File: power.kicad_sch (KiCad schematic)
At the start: 53 parts, among them J1 USB_C_Receptacle_USB2.0_16P, U1 TPS61088RHLT, U2 MCP73871, U3 AP2112K-3.3, U4 MAX17048G_T10, U5 USBLC6-2SC6

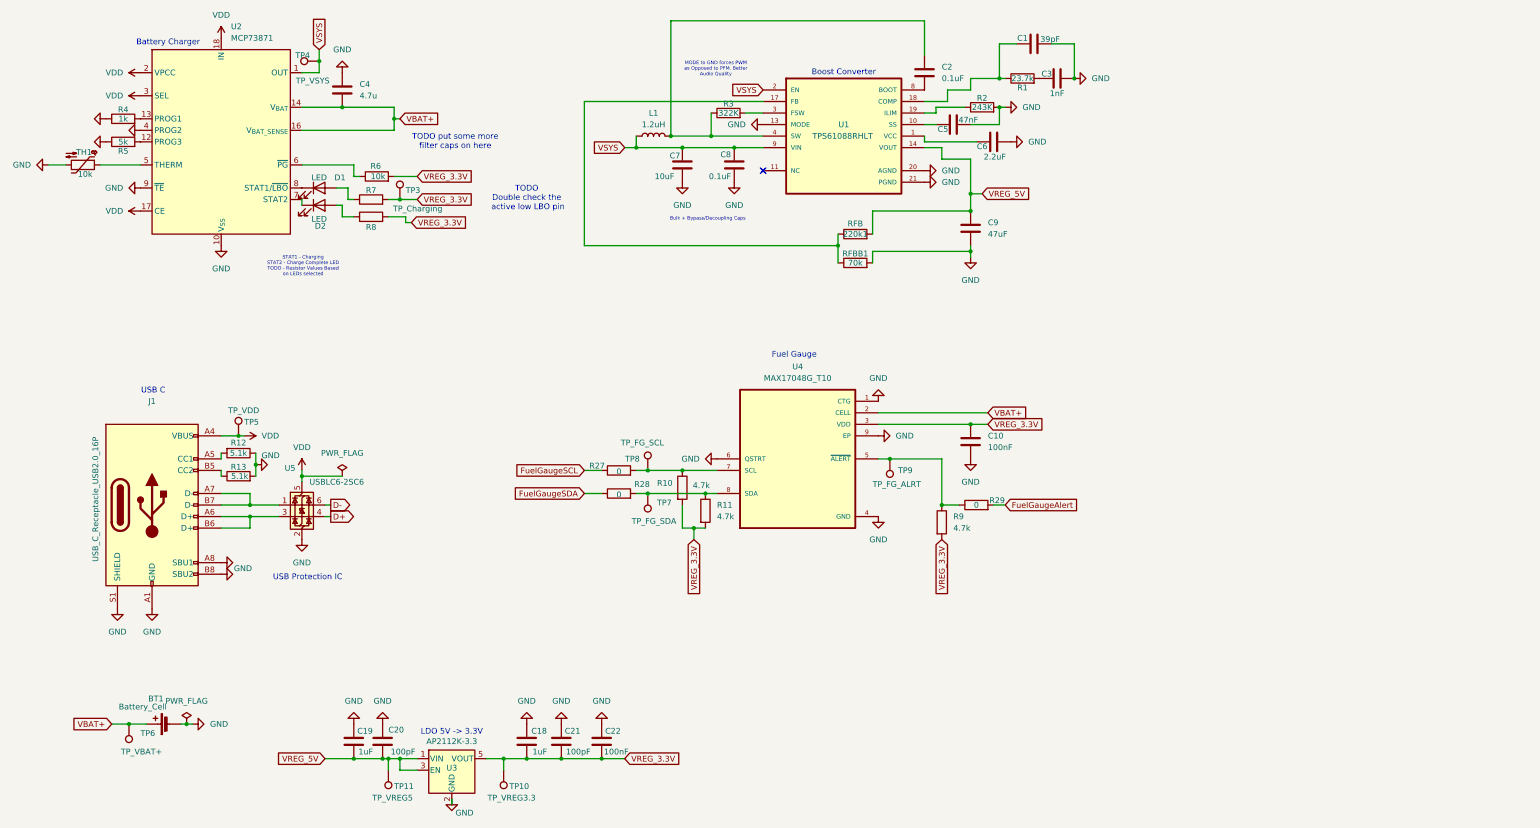
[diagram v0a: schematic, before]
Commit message: Remove Boost
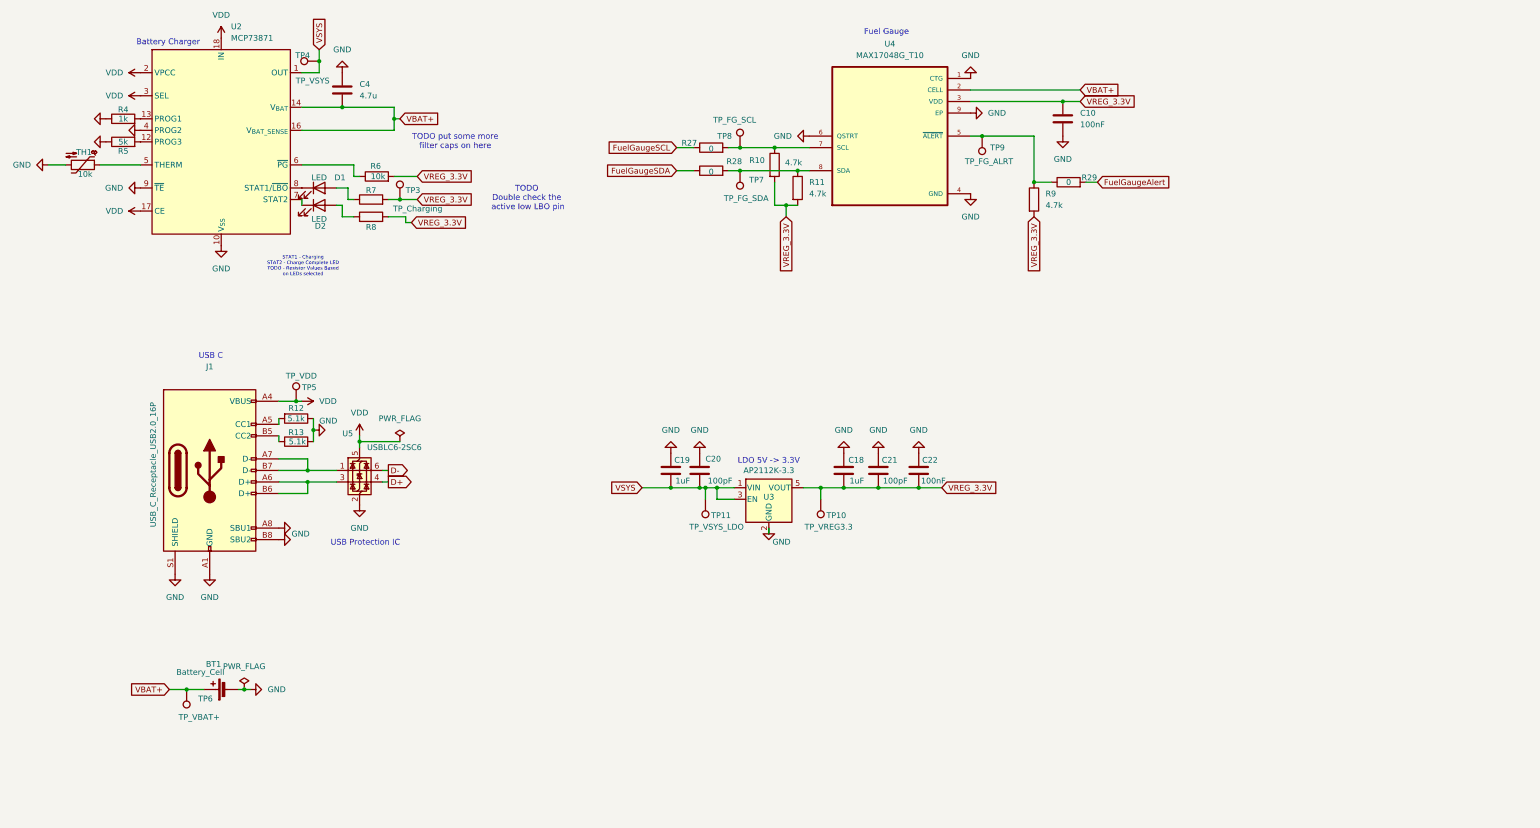
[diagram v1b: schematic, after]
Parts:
- removed 220k1: RFB, Resistor_SMD:R_0603_1608Metric_Pad0.98x0.95mm_HandSolder, symbol Device:R
- removed C1: 39pF, Capacitor_SMD:C_0603_1608Metric_Pad1.08x0.95mm_HandSolder, symbol Device:C
- removed C2, C8: 0.1uF, Capacitor_SMD:C_0603_1608Metric_Pad1.08x0.95mm_HandSolder, symbol Device:C
- removed C3: 1nF, Capacitor_SMD:C_0603_1608Metric_Pad1.08x0.95mm_HandSolder, symbol Device:C
- removed C5: 47nF, Capacitor_SMD:C_0603_1608Metric_Pad1.08x0.95mm_HandSolder, symbol Device:C
- removed C6: 2.2uF, Capacitor_SMD:C_0603_1608Metric_Pad1.08x0.95mm_HandSolder, symbol Device:C
- removed C7: 10uF, Capacitor_SMD:C_0603_1608Metric_Pad1.08x0.95mm_HandSolder, symbol Device:C
- removed C9: 47uF, Capacitor_SMD:C_0603_1608Metric_Pad1.08x0.95mm_HandSolder, symbol Device:C
- removed L1: 1.2uH, Inductor_SMD:L_0603_1608Metric_Pad1.05x0.95mm_HandSolder, symbol Device:L
- removed R1: 23.7k, Resistor_SMD:R_0603_1608Metric_Pad0.98x0.95mm_HandSolder, symbol Device:R
- removed R2: 243K, Resistor_SMD:R_0603_1608Metric_Pad0.98x0.95mm_HandSolder, symbol Device:R
- removed R3: 322K, Resistor_SMD:R_0603_1608Metric_Pad0.98x0.95mm_HandSolder, symbol Device:R
- removed RFBB1: 70k, Resistor_SMD:R_0603_1608Metric_Pad0.98x0.95mm_HandSolder, symbol Device:R
- removed U1: TPS61088RHLT, TPS61088RHLT:IC_MSP430FR2522IRHLR, symbol TPS61088:TPS61088RHLT
- TP11: value TP_VREG5 -> TP_VSYS_LDO
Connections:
- net VREG_5V is gone; now on net VSYS: C19.2, C20.2, TP11.1, U3.1 (VIN), U3.3 (EN)
- no-connect marks 1 -> 0
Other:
- note removed: "Boost Converter"
- note removed: "Bulk + Bypass/Decoupling Caps"
- note removed: "MODE to GND forces PWM as Opposed to PFM. Better Audio Quality"
- moved on the sheet: BT1, C10, C18, C19, C20, C21, C22, J1, R10, R11, R12, R13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

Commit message: Update USB C port and Charger to match App notes
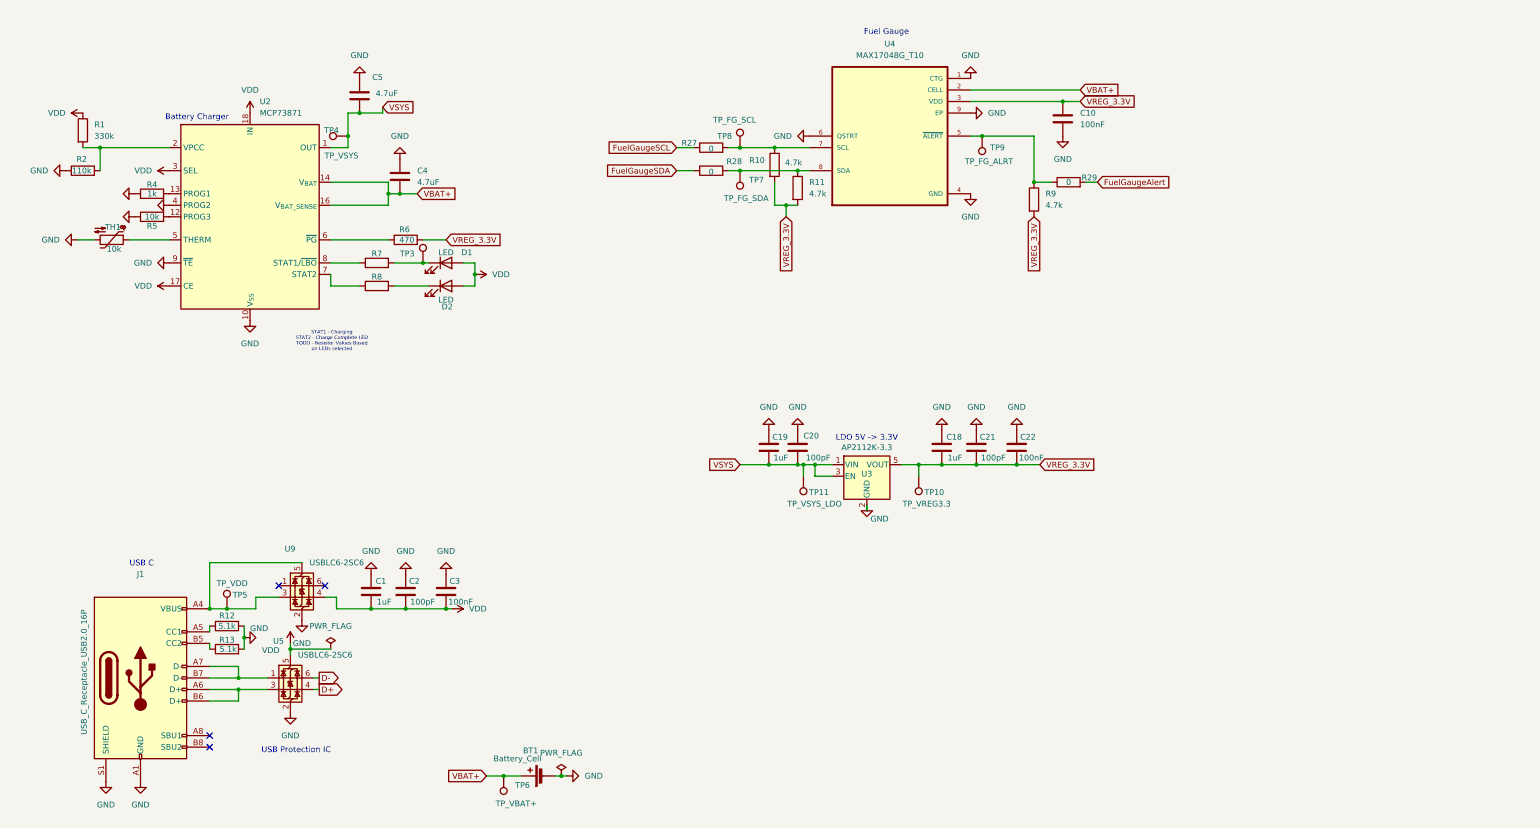
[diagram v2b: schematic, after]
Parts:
- added C1: 1uF, symbol Device:C
- added C2: 100pF, symbol Device:C
- added C3: 100nF, symbol Device:C
- added C5: 4.7uF, Capacitor_SMD:C_0603_1608Metric_Pad1.08x0.95mm_HandSolder, symbol Device:C
- added R1: 330k, symbol Device:R
- added R2: 110k, symbol Device:R
- added U9: USBLC6-2SC6, Package_TO_SOT_SMD:SOT-23-6, symbol Power_Protection:USBLC6-2SC6
- C4: value 4.7u -> 4.7uF
- R5: value 5k -> 10k
- R6: value 10k -> 470
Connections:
- net GND: now also C1.1, C2.1, C3.1, C5.2, R2.1, U9.2 (GND); no longer J1.A8 (SBU1), J1.B8 (SBU2)
- net VDD: now also D1.2 (A), D2.2 (A), C1.2, C2.2, C3.2, R1.1, U9.4 (I/O2); no longer J1.A4 (VBUS), J1.A9 (VBUS), J1.B4 (VBUS), J1.B9 (VBUS), TP5.1, U2.2 (VPCC)
- net VREG_3.3V: no longer R7.2, R8.2, TP3.1
- net VSYS: now also C5.1
- net at D1.1 (K): now also R7.2, TP3.1; no longer U2.8 (STAT1/~{LBO})
- net at R7.1: now also U2.8 (STAT1/~{LBO}); no longer D1.2 (A)
- net at D2.1 (K): now also R8.2; no longer U2.7 (STAT2)
- net at R8.1: now also U2.7 (STAT2); no longer D2.2 (A)
- new net: J1.A4 (VBUS), J1.A9 (VBUS), J1.B4 (VBUS), J1.B9 (VBUS), TP5.1, U9.3 (I/O2), U9.5 (VBUS)
- new net: R1.2, R2.2, U2.2 (VPCC)
- no-connect marks 0 -> 4
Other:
- note removed: "TODO Double check the active low LBO pin"
- note removed: "TODO put some more filter caps on here"
- moved on the sheet: BT1, C18, C19, C20, C21, C22, C4, D1, D2, J1, R12, R13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

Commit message: Finish power sheet
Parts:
- removed C10: 100nF, Capacitor_SMD:C_0603_1608Metric_Pad1.08x0.95mm_HandSolder, symbol Device:C
- removed C20: 100pF, symbol Device:C
- added C6: 0.1uF, Capacitor_SMD:C_0603_1608Metric_Pad1.08x0.95mm_HandSolder, symbol Device:C
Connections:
- net GND: now also C6.2
- net VBAT+: now also U4.3 (VDD), C6.1
- net VREG_3.3V: no longer U4.3 (VDD)

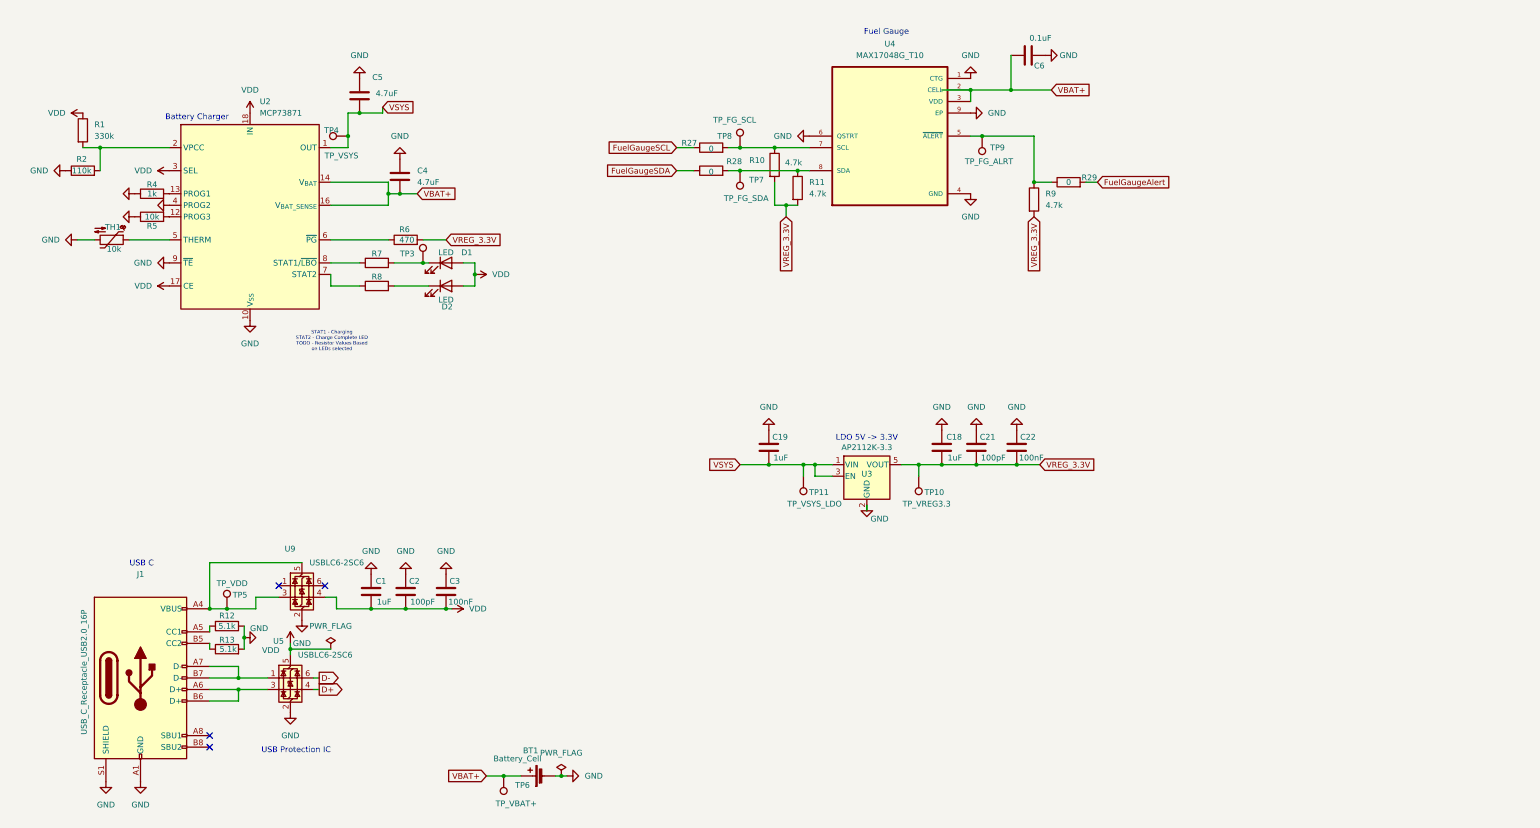
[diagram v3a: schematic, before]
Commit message: Update the USB-C symbol to match the actual part
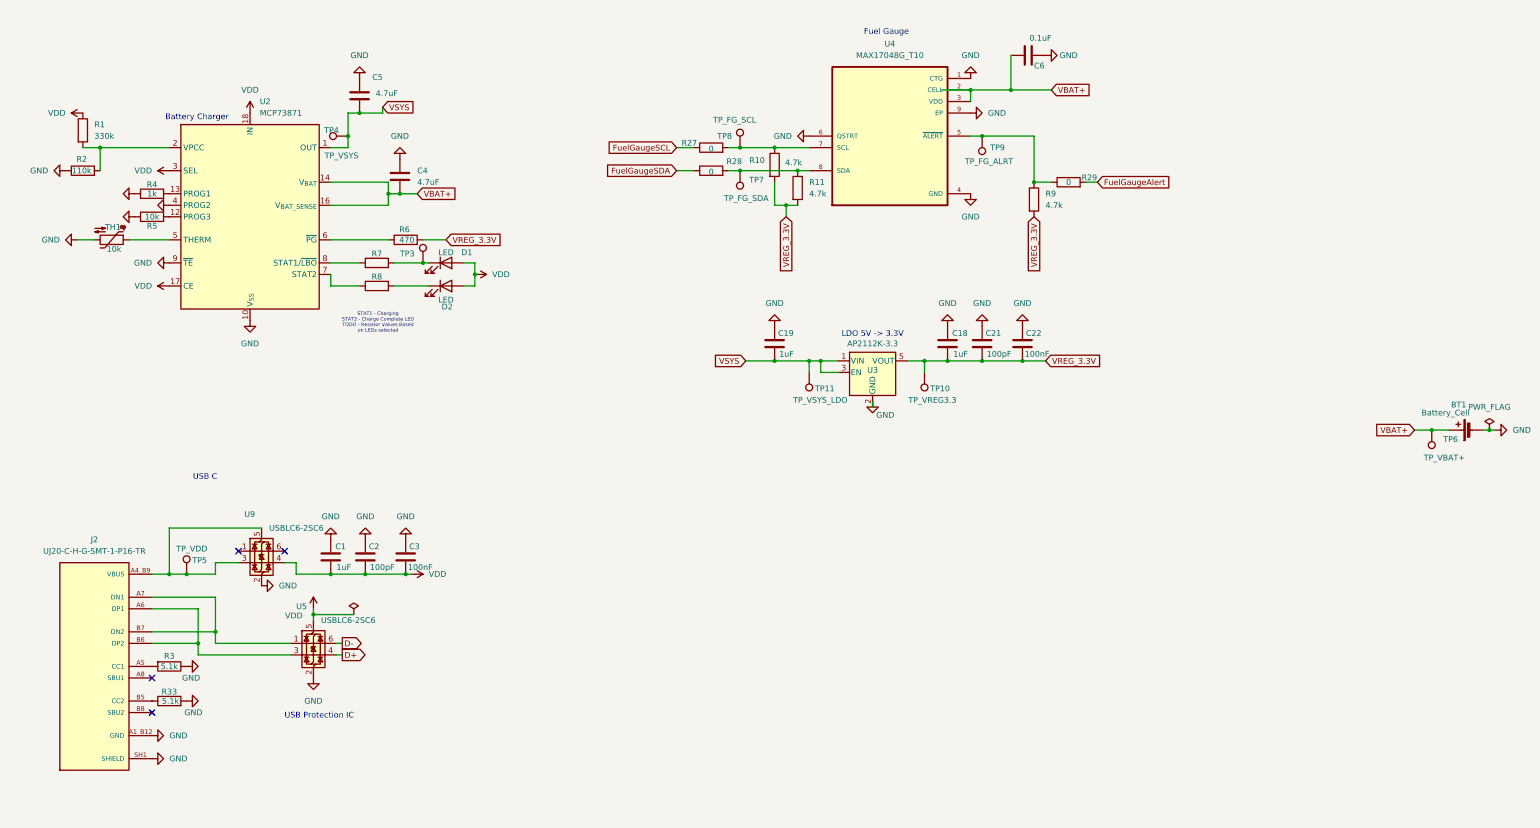
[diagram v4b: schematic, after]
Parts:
- removed J1: USB_C_Receptacle_USB2.0_16P, UJ20-C-H-G-SMT-1-P16-TR:SAMESKY_UJ20-C-H-G-SMT-1-P16-TR, symbol Connector:USB_C_Receptacle_USB2.0_16P
- removed R12, R13: 5.1k, Resistor_SMD:R_0603_1608Metric_Pad0.98x0.95mm_HandSolder, symbol Device:R
- added J2: UJ20-C-H-G-SMT-1-P16-TR, UJ20-C-H-G-SMT-1-P16-TR:SAMESKY_UJ20-C-H-G-SMT-1-P16-TR, symbol UJ20-C-H-G-SMT-1-P16-TR:UJ20-C-H-G-SMT-1-P16-TR
- added R3, R33: 5.1k, Resistor_SMD:R_0603_1608Metric_Pad0.98x0.95mm_HandSolder, symbol Device:R
- C1, C18, C19, C2, C21, C22, C3: footprint (none) -> Capacitor_SMD:C_0603_1608Metric_Pad1.08x0.95mm_HandSolder
- R1, R2, R27, R28, R29: footprint (none) -> Resistor_SMD:R_0603_1608Metric_Pad0.98x0.95mm_HandSolder
- TP10, TP11, TP3, TP4, TP5, TP6, TP7, TP8, TP9: footprint (none) -> TestPoint:TestPoint_Pad_D2.5mm
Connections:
- net GND: now also J2.A1_B12 (GND), J2.B1_A12 (GND), J2.SH1 (SHIELD), J2.SH2 (SHIELD), J2.SH3 (SHIELD), J2.SH4 (SHIELD), R3.1, R33.2
- net at TP5.1, U9.3 (I/O2), U9.5 (VBUS): now also J2.A4_B9 (VBUS), J2.B4_A9 (VBUS)
- net at U5.3 (I/O2): now also J2.A6 (DP1), J2.B6 (DP2)
- net at U5.1 (I/O1): now also J2.A7 (DN1), J2.B7 (DN2)
- new net: J2.A5 (CC1), R3.2
- new net: J2.B5 (CC2), R33.1
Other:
- moved on the sheet: BT1, C1, C18, C19, C2, C21, C22, C3, TP10, TP11, TP5, TP6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

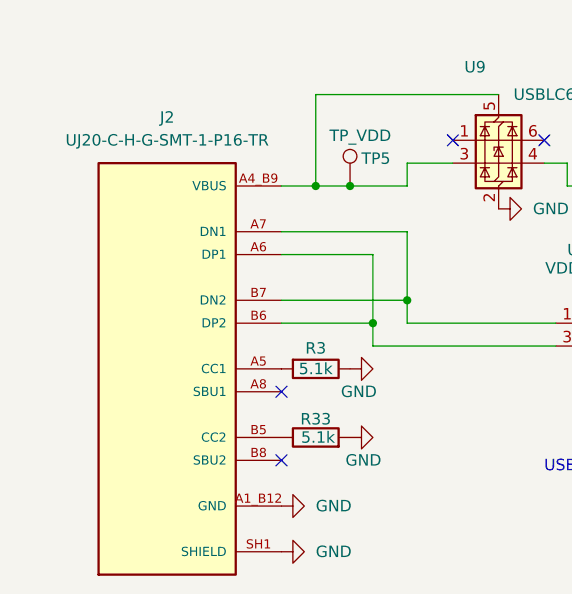
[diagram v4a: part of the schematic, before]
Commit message: Put component families together on PCB
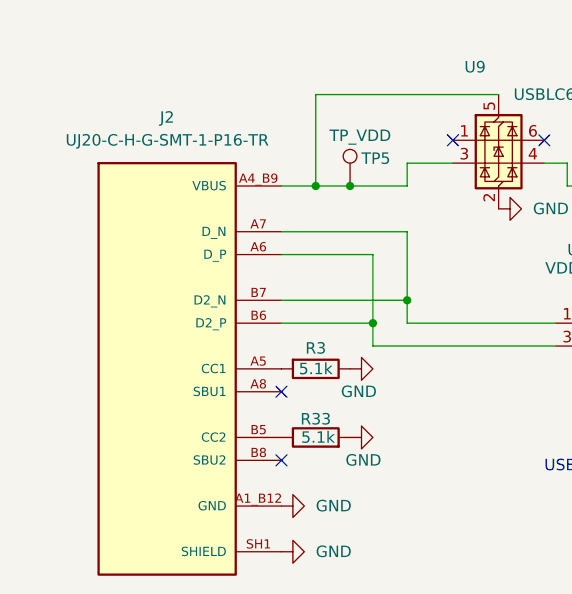
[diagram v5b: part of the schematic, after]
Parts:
- TP10, TP11, TP3, TP4, TP5, TP6, TP7, TP8, TP9: footprint TestPoint:TestPoint_Pad_D2.5mm -> TestPoint:TestPoint_Pad_D1.5mm
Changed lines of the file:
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@@
 			)
 		)
-		(property "Footprint" "TestPoint:TestPoint_Pad_D2.5mm"
+		(property "Footprint" "TestPoint:TestPoint_Pad_D1.5mm"
 			(at 186.69 93.98 0)
 			(effects
@@
 			)
 		)
-		(property "Footprint" "TestPoint:TestPoint_Pad_D2.5mm"
+		(property "Footprint" "TestPoint:TestPoint_Pad_D1.5mm"
 			(at 224.79 41.91 0)
 			(effects
@@
 			)
 		)
-		(property "Footprint" "TestPoint:TestPoint_Pad_D2.5mm"
+		(property "Footprint" "TestPoint:TestPoint_Pad_D1.5mm"
 			(at 59.69 138.43 0)
 			(effects
@@
 			)
 		)
-		(property "Footprint" "TestPoint:TestPoint_Pad_D2.5mm"
+		(property "Footprint" "TestPoint:TestPoint_Pad_D1.5mm"
 			(at 181.61 44.45 0)
 			(effects
@@
 			)
 		)
-		(property "Footprint" "TestPoint:TestPoint_Pad_D2.5mm"
+		(property "Footprint" "TestPoint:TestPoint_Pad_D1.5mm"
 			(at 171.45 49.53 0)
 			(effects
@@
 			)
 		)
-		(property "Footprint" "TestPoint:TestPoint_Pad_D2.5mm"
+		(property "Footprint" "TestPoint:TestPoint_Pad_D1.5mm"
 			(at 111.76 69.85 0)
 			(effects
@@
 			)
 		)
-		(property "Footprint" "TestPoint:TestPoint_Pad_D2.5mm"
+		(property "Footprint" "TestPoint:TestPoint_Pad_D1.5mm"
 			(at 212.09 93.98 0)
 			(effects
@@
 			)
 		)
-		(property "Footprint" "TestPoint:TestPoint_Pad_D2.5mm"
+		(property "Footprint" "TestPoint:TestPoint_Pad_D1.5mm"
 			(at 323.85 106.68 0)
 			(effects
@@
 			)
 		)
-		(property "Footprint" "TestPoint:TestPoint_Pad_D2.5mm"
+		(property "Footprint" "TestPoint:TestPoint_Pad_D1.5mm"
 			(at 90.17 36.83 0)
 			(effects
